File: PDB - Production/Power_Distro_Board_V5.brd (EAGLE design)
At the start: 63.6 x 116.9 mm, 64 parts

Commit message: added PDB production files
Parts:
- removed ROT_STEP, U$2: 555X-3, con-molex-2:5566-3
- moved 12V_TEST 12.5 mm to (21.8, 96.1)
- moved 5V_TEST1 11.9 mm to (26.1, 57.1)
- moved F10 10.2 mm to (38.1, 8.89), turned to 0 degrees
- moved R1 8.28 mm to (22.2, 107.4)
- moved 5A 8.27 mm to (11.7, 68.2)
- moved F8 6.99 mm to (15.5, 87.4), turned to 0 degrees
- moved POWER 6.93 mm to (3.82, 105.3)
- moved C9 6.54 mm to (19.6, 51.5)
- moved C7 6.41 mm to (13.2, 51.5)
- moved F9 6.19 mm to (19.6, 46.4)
- moved EN 6.15 mm to (4.18, 52.0)
- moved R10 5.93 mm to (19.6, 40.0)
- moved U$1 5.76 mm to (10.4, 105.5)
- moved RVP_1 5.08 mm to (35.6, 106.7)
- moved 5V_RAIL 4.61 mm to (9.39, 40.0)
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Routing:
- net N$3: track 0.00 -> 16.7 mm
- net GND: track 0.00 -> 12.2 mm, vias 0 -> 1
- added copper zone on layer 16, net GND

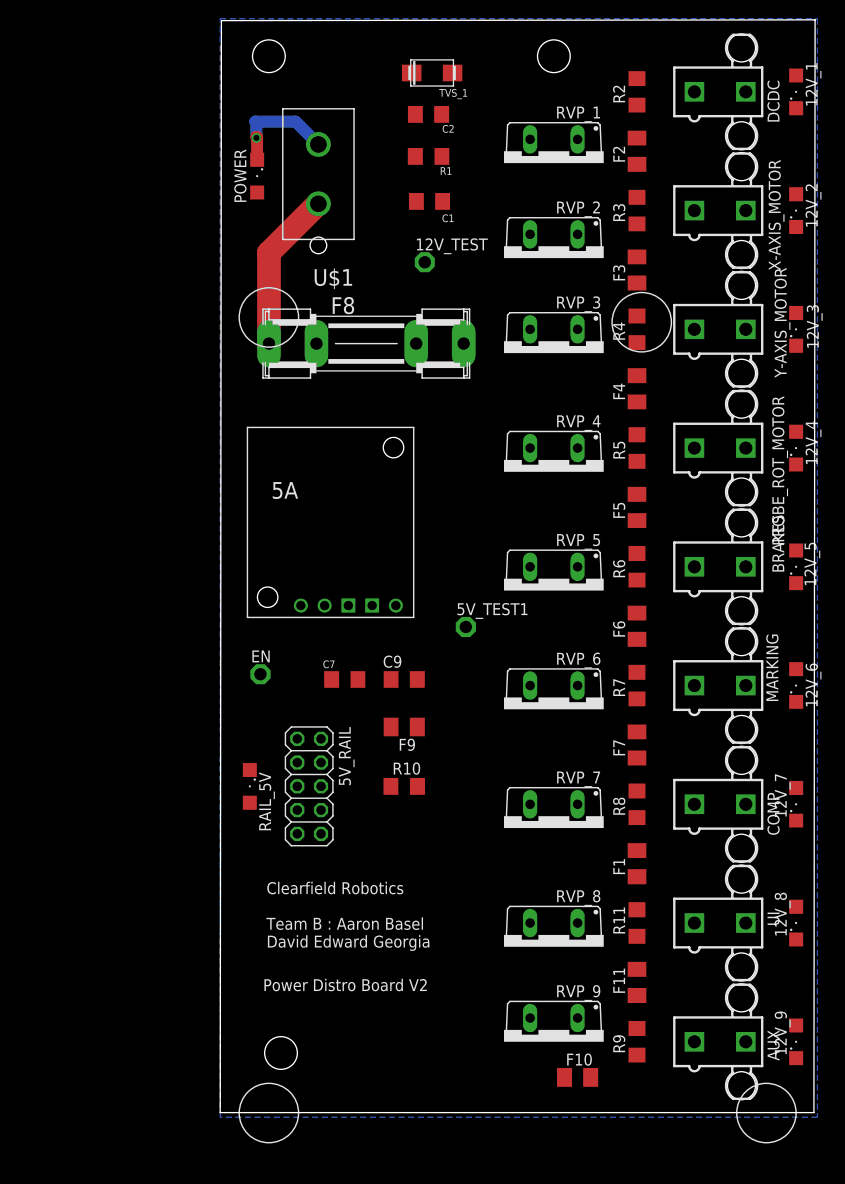
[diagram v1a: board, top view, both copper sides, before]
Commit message: Routed PDB
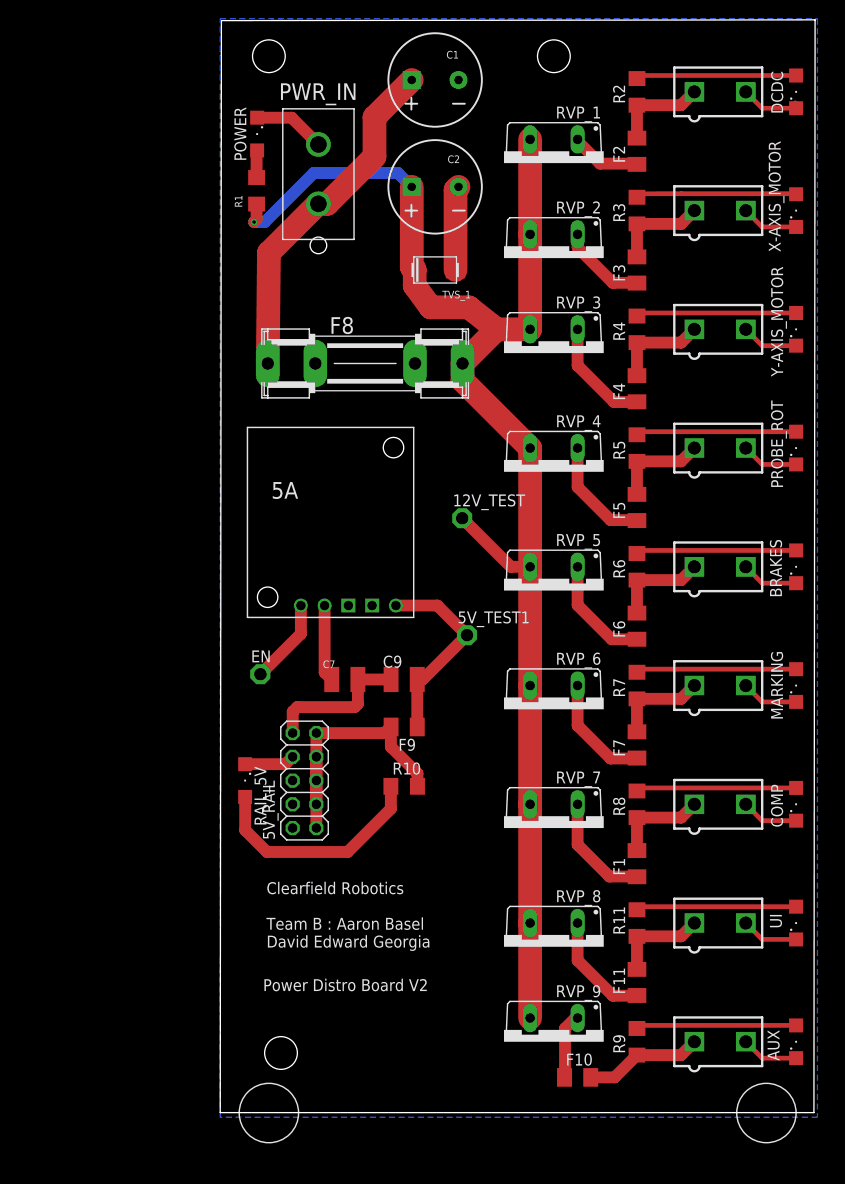
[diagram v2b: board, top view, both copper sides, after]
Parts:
- C1, C2: device resistor:C1206 -> SparkFun-Capacitors:CPOL-RADIAL-5MM-10MM
- C7, C9: device resistor:C1206 -> eagle-ltspice:C1210
- F1, F11: value 60VDC 20A -> 5A
- F10, F2, F3, F4, F5, F6, F7: value 60VDC 20A -> 20A
- F8: value (none) -> 30A
- moved 12V_TEST 27.7 mm to (25.8, 68.7)
- moved TVS_1 21.1 mm to (22.9, 95.2)
- moved R1 18.8 mm to (3.76, 103.7), turned to 90 degrees
- moved C1 13.0 mm to (22.9, 115.6)
- moved C2 7.78 mm to (22.9, 104.1)
- moved POWER 4.50 mm to (3.82, 109.8)
- moved F8 2.13 mm to (15.4, 85.2)
- moved 5V_TEST1 0.88 mm to (26.3, 56.2)
- moved 5V_RAIL 0.80 mm to (8.89, 40.6), turned to 90 degrees
- moved RAIL_5V 0.80 mm to (2.54, 40.6)
- renumbered PROBE_ROT_MOTOR to PROBE_ROT, U$1 to PWR_IN
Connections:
- net 12V_REG1: now also C2.+; no longer C2.2
- net GND: now also C1.-, C2.-, DCDC.2; no longer C1.1, C2.1, DCDC.1
- net N$12: now also DCDC.1; no longer DCDC.2
- net N$3: now also C1.+; no longer C1.2
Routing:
- net 12V_REG1: track 0.00 -> 154.6 mm, vias 0 -> 1
- net GND: track 12.2 -> 93.5 mm, vias 1 -> 0
- net 5V_REG3: track 0.00 -> 31.2 mm
- net N$11: track 0.00 -> 24.4 mm
- net N$32: track 0.00 -> 21.3 mm
- net N$3: track 16.7 -> 37.2 mm
- net N$16: track 0.00 -> 17.4 mm
- net N$9: track 0.00 -> 17.2 mm
- net N$29: track 0.00 -> 17.2 mm
- net N$27: track 0.00 -> 17.2 mm
- net N$24: track 0.00 -> 17.2 mm
- net N$13: track 0.00 -> 17.2 mm
- net N$33: track 0.00 -> 17.2 mm
- net N$21: track 0.00 -> 17.2 mm
- net N$15: track 0.00 -> 17.2 mm
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
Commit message: PDB fatter routes, dimension good, top ground plane
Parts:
- moved PWR_IN 9.64 mm to (12.0, 96.0)
- moved POWER 9.38 mm to (3.82, 100.4)
- moved R1 9.38 mm to (3.76, 94.3)
- moved 5A 5.13 mm to (11.8, 63.1)
- moved RVP_7 5.13 mm to (35.7, 30.4)
- moved 12V_1 5.13 mm to (61.6, 109.2)
- moved 12V_2 5.13 mm to (61.6, 96.5)
- moved 12V_3 5.13 mm to (61.6, 83.8)
- moved 12V_4 5.13 mm to (61.6, 71.1)
- moved 12V_5 5.13 mm to (61.6, 58.4)
- moved 12V_6 5.13 mm to (61.6, 45.7)
- moved 12V_7 5.13 mm to (61.6, 33.0)
- moved 12V_8 5.13 mm to (61.6, 20.3)
- moved 12V_TEST 5.13 mm to (25.9, 63.6)
- moved 5V_RAIL 5.13 mm to (9.02, 35.5)
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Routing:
- net N$3: track 37.2 -> 45.6 mm
- net N$29: track 17.2 -> 20.2 mm
- net N$33: track 17.2 -> 20.0 mm
- net N$24: track 17.2 -> 19.9 mm
- net 5V_REG3: track 31.2 -> 28.5 mm
- net N$15: track 17.2 -> 19.5 mm
- net N$27: track 17.2 -> 19.5 mm
- net N$21: track 17.2 -> 19.4 mm
- net 12V_REG1: track 154.6 -> 156.8 mm, vias 1 -> 0
- net N$9: track 17.2 -> 19.3 mm
- net N$16: track 17.4 -> 19.4 mm
- net N$13: track 17.2 -> 18.9 mm
- net GND: track 93.5 -> 95.1 mm, vias 0 -> 17
- net N$5: track 7.57 -> 8.25 mm
- net N$26: track 12.0 -> 12.6 mm
- added copper zone on layer 1, net GND
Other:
- board size 63.6 x 116.9 mm -> 63.5 x 116.8 mm
- board text added: "// Clearfield R b tics Team B : Aar n Basel David Edward Ge rgia"
- board text added: "P wer Distr B ard V2"
- board text removed: "Clearfield Robotics Team B : Aaron Basel David Edward Georgia"
- board text removed: "Power Distro Board V2"

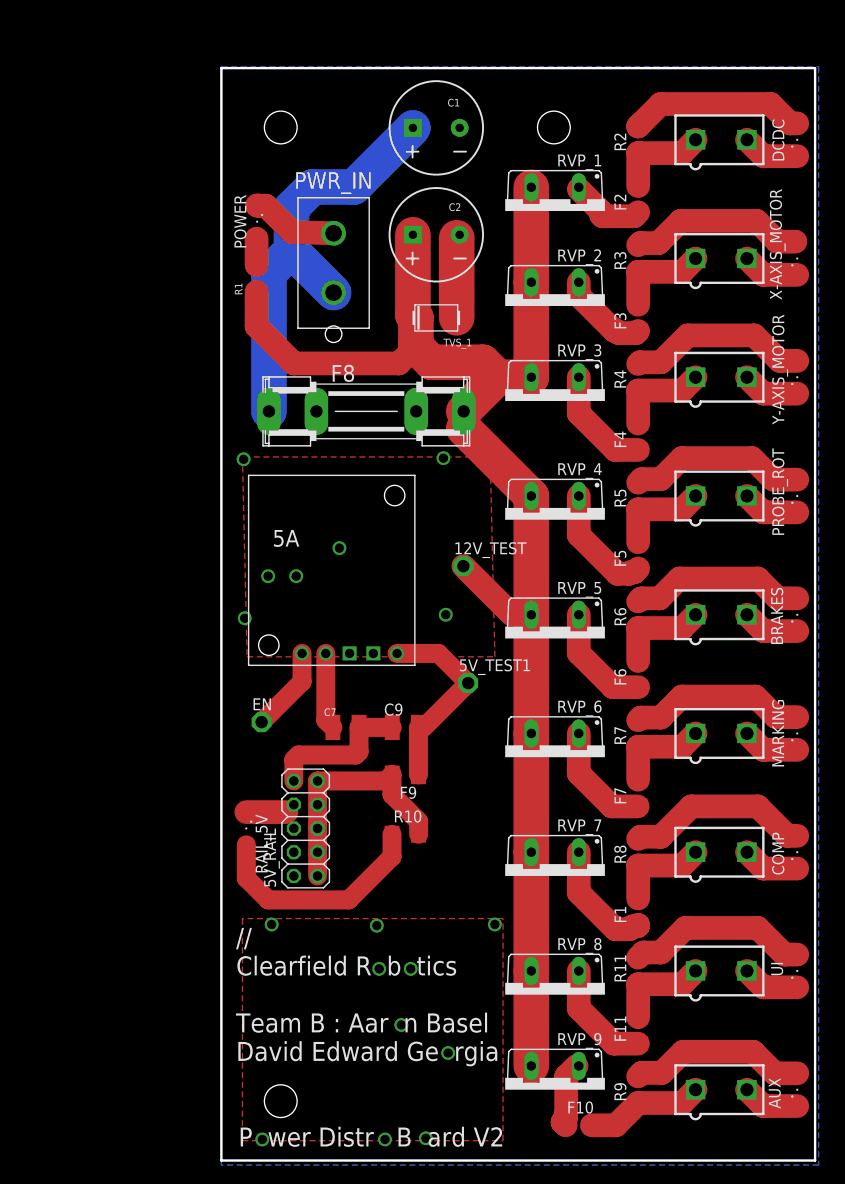
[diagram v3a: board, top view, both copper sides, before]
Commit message: Updated PDB and Gerber files for US manufacturers
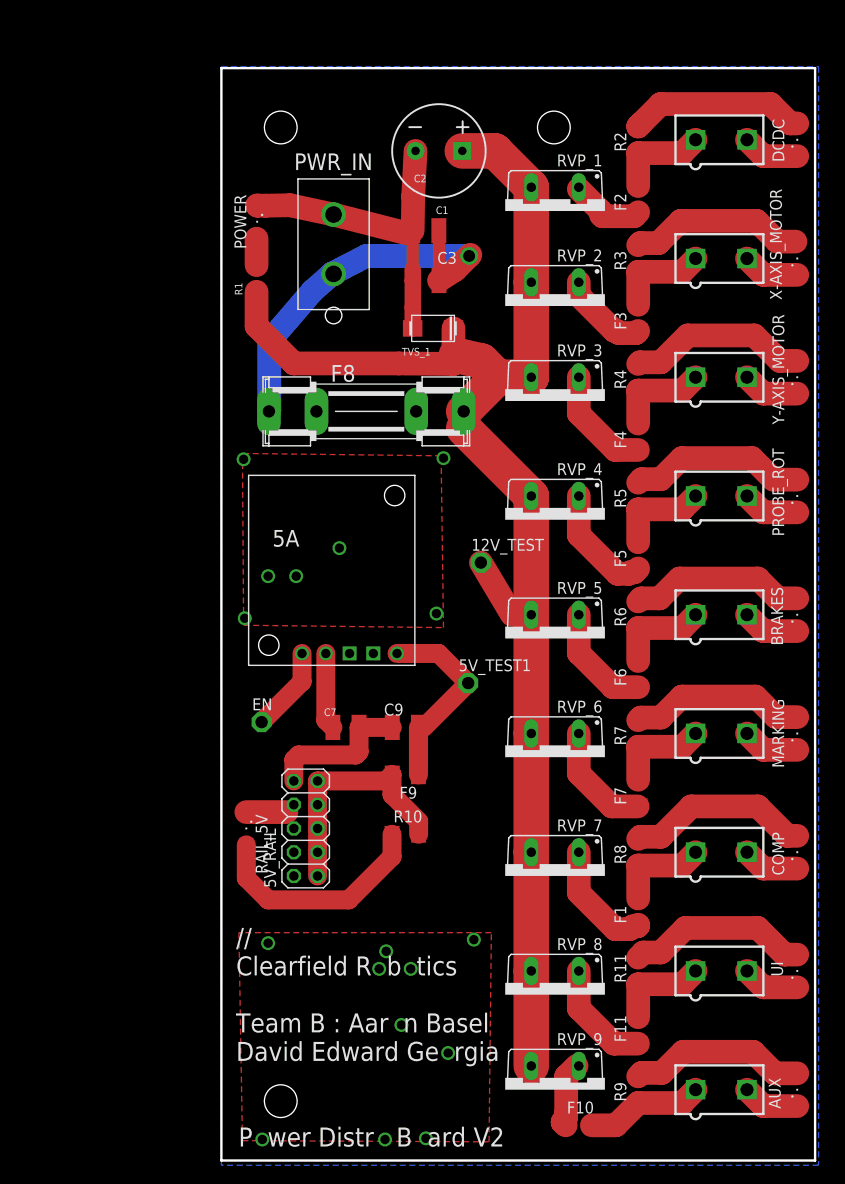
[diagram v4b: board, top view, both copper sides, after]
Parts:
- added C3: 100nF, eagle-ltspice:C1210
- C1: device SparkFun-Capacitors:CPOL-RADIAL-5MM-10MM -> eagle-ltspice:C1210
- C2: value 100nF -> 250uF
- moved C1 11.1 mm to (21.9, 99.4)
- moved C2 8.97 mm to (23.3, 108.0), turned to 0 degrees
- moved PWR_IN 2.00 mm to (12.0, 98.0)
- moved 12V_TEST 1.91 mm to (27.8, 64.0)
- moved TVS_1 1.18 mm to (22.6, 89.0), turned to 180 degrees
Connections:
- net GND: now also C1.2, C3.1; no longer C1.-
- net N$3: now also C1.1, C3.2; no longer C1.+
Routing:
- net GND: track 95.1 -> 112.8 mm
- net N$3: track 45.6 -> 43.2 mm, vias 0 -> 1
- net 12V_REG1: track 156.8 -> 156.0 mm
